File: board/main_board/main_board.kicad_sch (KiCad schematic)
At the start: 12 parts, among them J1 Sphygmomanometer, J2 ServorMotor0, J3 TemperatureSensor, J4 Oximeter, J5 Source, J6 ServorMotor1, J7 RaspSPI, U1 STM32F411CCYx, U2 ADuM1300xRW, U3 ADuM1411

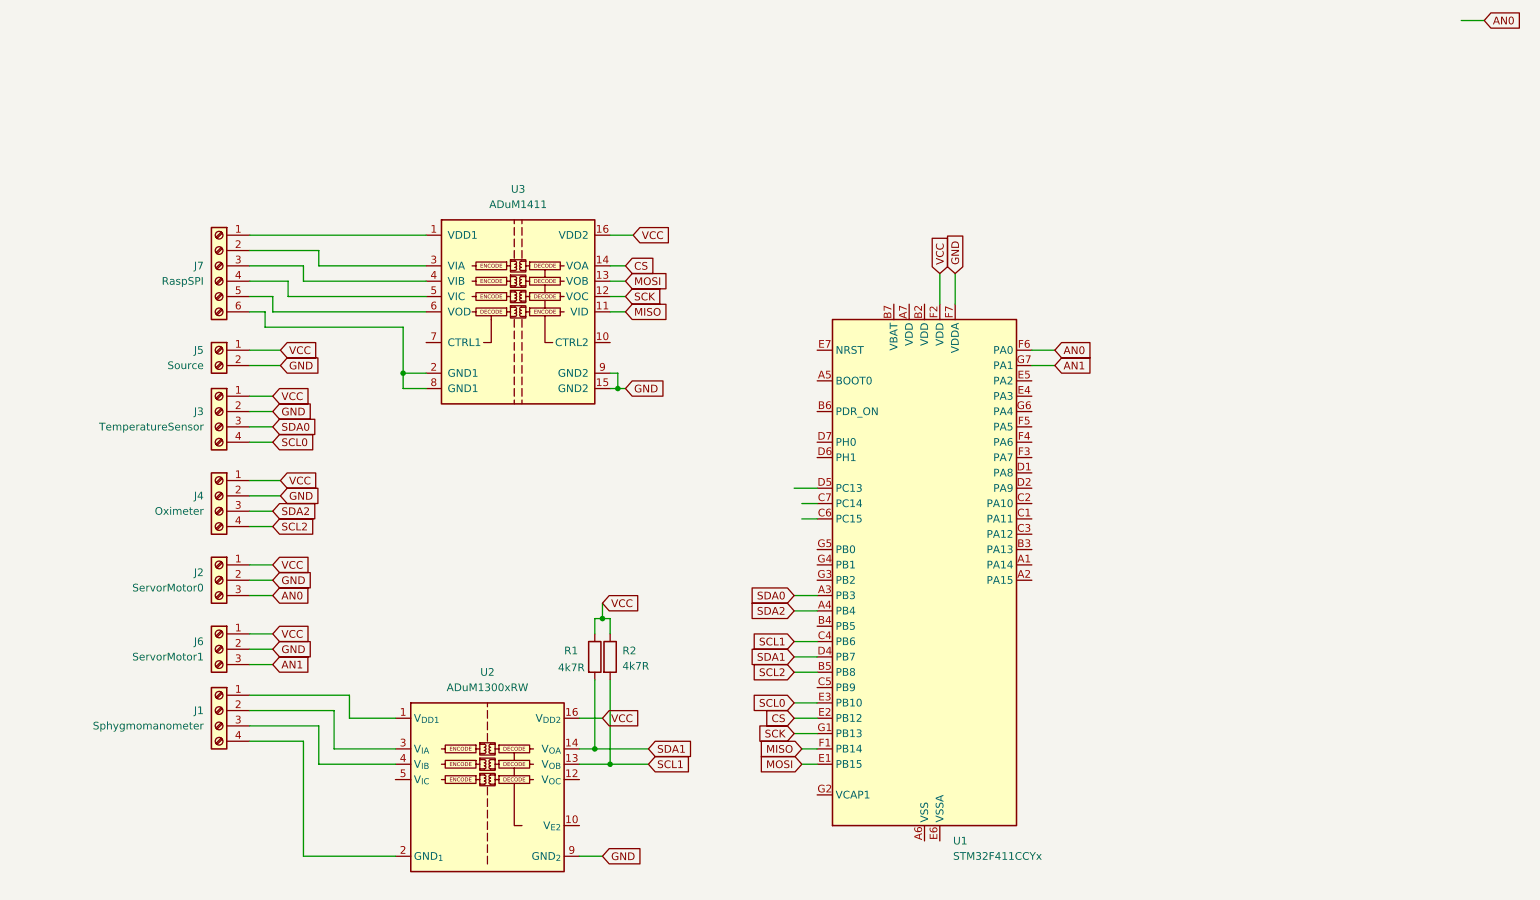
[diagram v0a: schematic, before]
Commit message: refactor: update board schematic
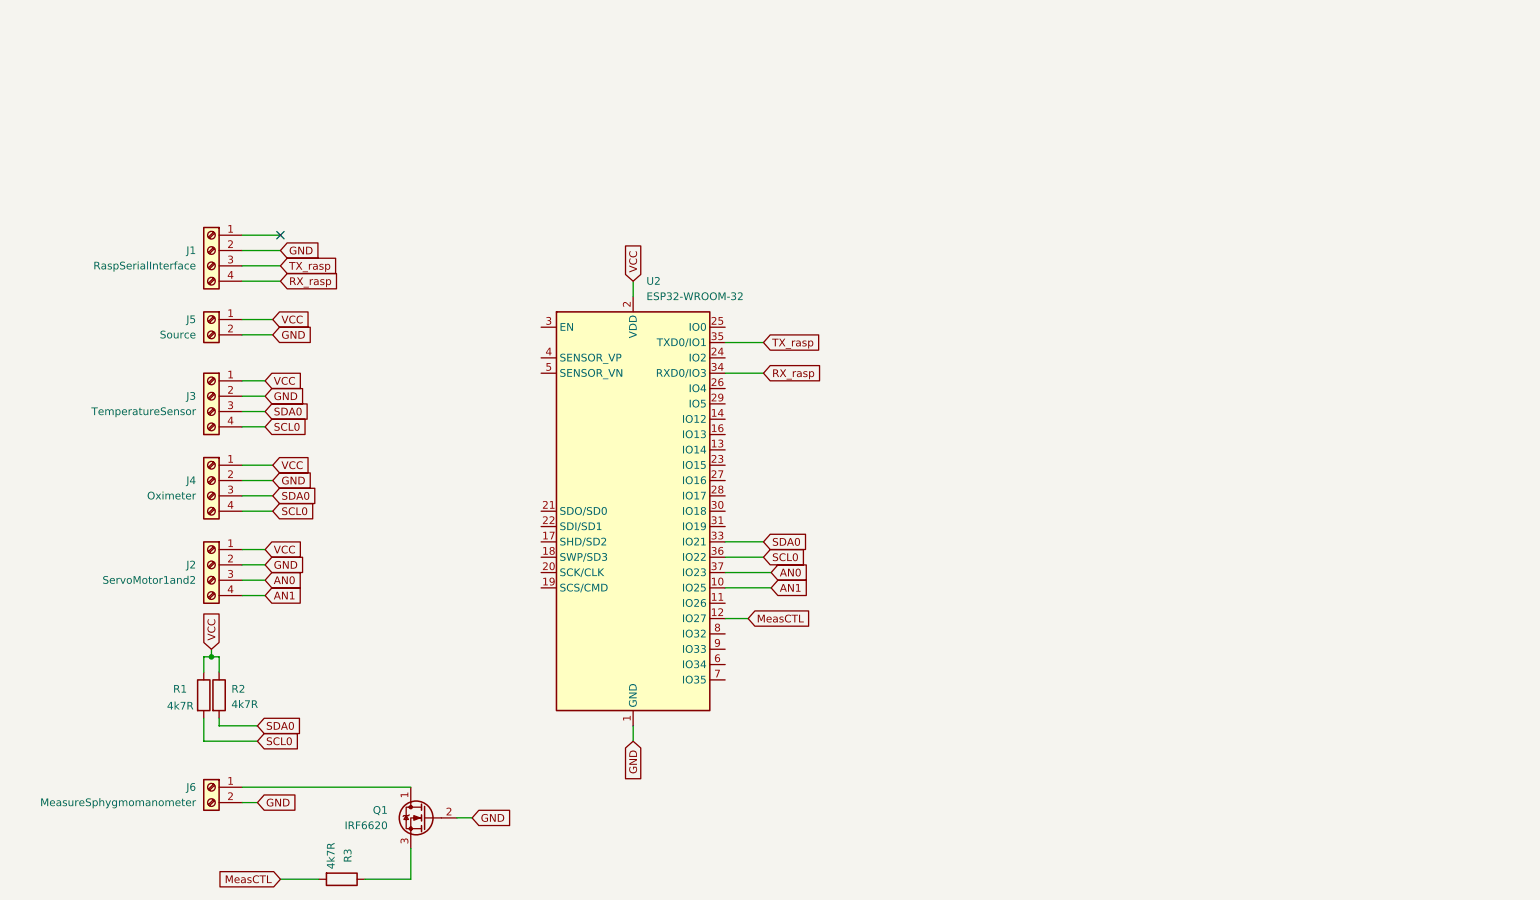
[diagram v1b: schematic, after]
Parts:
- removed J2: ServorMotor0, symbol Connector:Screw_Terminal_01x03
- removed J6: ServorMotor1, symbol Connector:Screw_Terminal_01x03
- removed J7: RaspSPI, symbol Connector:Screw_Terminal_01x06
- removed U1: STM32F411CCYx, Package_CSP:ST_WLCSP-49_Die431, symbol MCU_ST_STM32F4:STM32F411CCYx
- removed U2: ADuM1300xRW, Package_SO:SOIC-16W_7.5x10.3mm_P1.27mm, symbol Isolator:ADuM1300xRW
- removed U3: ADuM1411, Package_SO:SOIC-16W_7.5x10.3mm_P1.27mm, symbol Isolator:ADuM1411
- added J2: ServoMotor1and2, symbol Connector:Screw_Terminal_01x04
- added J6: MeasureSphygmomanometer, symbol Connector:Screw_Terminal_01x02
- added Q1: IRF6620, Package_DirectFET:DirectFET_MX, symbol Transistor_FET:IRF6620
- added R3: 4k7R, symbol Device:R
- added U2: ESP32-WROOM-32, RF_Module:ESP32-WROOM-32, symbol RF_Module:ESP32-WROOM-32
- J1: value Sphygmomanometer -> RaspSerialInterface
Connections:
- net SCL1 is gone; now on net SDA0: R2.2
- net SCL2 is gone; now on net SCL0: J4.4 (Pin_4)
- net SDA1 is gone; now on net SCL0: R1.2
- net SDA2 is gone; now on net SDA0: J4.3 (Pin_3)
- net AN0: now also J2.3 (Pin_3), U2.37 (IO23)
- net AN1: now also J2.4 (Pin_4), U2.10 (IO25)
- net GND: now also J1.2 (Pin_2), J2.2 (Pin_2), J6.2 (Pin_2), Q1.2 (G), U2.1 (GND), U2.15 (GND), U2.38 (GND), U2.39 (GND)
- net SCL0: now also U2.36 (IO22)
- net SDA0: now also U2.33 (IO21)
- net VCC: now also J2.1 (Pin_1), U2.2 (VDD)
- net TX_rasp: now reaches J1.3 (Pin_3)
- net TX_rasp: now also U2.35 (TXD0/IO1)
- net RX_rasp: now reaches J1.4 (Pin_4)
- net RX_rasp: now also U2.34 (RXD0/IO3)
- new net: J6.1 (Pin_1), Q1.1 (D)
- new net: Q1.3 (S), R3.1
- new net MeasCTL: R3.2, U2.12 (IO27)
- no-connect marks 0 -> 1
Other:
- moved on the sheet: J3, J4, J5, R1, R2
